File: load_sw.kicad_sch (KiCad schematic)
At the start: 47 parts, among them Q10 2N7002 TR PBFREE, Q11 MMBT3904, Q12 2N7002 TR PBFREE, Q4 2N7002 TR PBFREE, Q5 MMBT3904, Q6 2N7002 TR PBFREE, Q7 2N7002 TR PBFREE, Q8 MMBT3904, Q9 PSMN020-100YS, U10 LM5050-1, U9 TPS16851VMAR

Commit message: Working on layout
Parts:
- removed TP2: TP_PGOOD, TestPoint:TestPoint_Plated_Hole_D5.0mm, symbol Connector:TestPoint
- removed TP3: TP_FLTn, TestPoint:TestPoint_Plated_Hole_D5.0mm, symbol Connector:TestPoint

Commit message: Working on it
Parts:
- renumbered D1 to D3, D2 to D4, D3 to D5, D4 to D6, D5 to D7, D6 to D8, D7 to D9, Q11 to Q10, Q12 to Q11, Q4 to Q3, Q5 to Q4, Q6 to Q5, Q7 to Q6, Q8 to Q7, Q9 to Q8, Q10 to Q9, R27 to R25, R28 to R26, R29 to R27, R30 to R28, R31 to R29, R32 to R30, R33 to R31, R34 to R32, R35 to R33, R36 to R34, R37 to R35, R38 to R36, R39 to R37, R40 to R38, R41 to R39, R42 to R40, R43 to R41, R44 to R42, R45 to R43

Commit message: Working on schematic and layout
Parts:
- removed D5: LTST-C190KRKT, LED_SMD:LED_0603_1608Metric, symbol Device:LED
- removed D7: LTST-C170GKT, LED_SMD:LED_0805_2012Metric, symbol Device:LED
- removed D9: LTST-C190KFKT, LED_SMD:LED_0603_1608Metric, symbol Device:LED
- removed Q10, Q4, Q7: MMBT3904, Package_TO_SOT_SMD:TSOT-23, symbol Device:Q_NPN
- removed Q11, Q3, Q5, Q6, Q9: 2N7002 TR PBFREE, Package_TO_SOT_SMD:TSOT-23, symbol Transistor_FET:Q_NMOS_DGS
- removed R36, R38, R42: 1Meg, Resistor_SMD:R_0603_1608Metric, symbol Device:R_US
- removed R37, R40, R43: 21.5, Resistor_SMD:R_0603_1608Metric, symbol Device:R_US
- added Q3: 2N7002, Package_TO_SOT_SMD:SOT-23, symbol Transistor_FET:2N7002
- added R37: R, symbol Device:R
- U10: renamed from U9; Supplier_2 (none) -> JLCPCB; Supplier_2 P/N (none) -> C52742265; Supplier_2 Price @ Qty (none) -> 1; Supplier_2 Unit Price (none) -> 11.0758
- renumbered C58 to C60, C59 to C61, C60 to C62, C61 to C63, C62 to C64, C63 to C65, C64 to C66, C65 to C67, R25 to R26, R26 to R27, R27 to R28, R28 to R29, R29 to R30, R30 to R31, R31 to R32, R32 to R33, R33 to R34, R34 to R35, R35 to R36, R39 to R40, R41 to R42, U10 to U11
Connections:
- net EN: now also Q3.1 (G), R37.1
- net EN_UVLO: now also Q3.3 (D)
- net GND: now also Q3.2 (S), R37.2
- net SWEN: now reaches U10.20 (SWEN)
- no-connect marks 5 -> 4

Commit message: BOM in folder
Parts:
- removed R37: R, symbol Device:R
- added R24: 10k, Resistor_SMD:R_0603_1608Metric, symbol Device:R
- C60, C65: Supplier_1 Digikey -> LCSC; Supplier_1 P/N 490-GCM1885C2A101FA16DTR-ND -> C527967; Supplier_1 Unit Price 0.14000 -> (none)
- C61: JLCPCB Status (none) -> JLC in-stock package match; Mfr P/N GCM1885C2A100FA16D -> CL10C100JB8NNNC; Supplier_1 Digikey -> LCSC; Supplier_1 P/N 490-GCM1885C2A100FA16DTR-ND -> C1634; Supplier_1 Unit Price 0.14000 -> (none)
- C62: JLCPCB Status (none) -> JLC in-stock package match; Mfr P/N CC0603JRX7R9BB224 -> CL10B224KA8NNNC; Supplier_1 Digikey -> LCSC; Supplier_1 P/N 13-CC0603JRX7R9BB224TR-ND -> C21120; Supplier_1 Unit Price 0.15000 -> (none)
- C63: JLCPCB Status (none) -> JLC in-stock package match; Mfr P/N GCM1885C1H472FA16D -> 0603B472K500NT; Supplier_1 Digikey -> LCSC; Supplier_1 P/N 490-GCM1885C1H472FA16DTR-ND -> C53987; Supplier_1 Unit Price 0.18000 -> (none)
- C64: JLCPCB Status (none) -> JLC in-stock package match; Mfr P/N GCM1885C2A220FA16D -> CL10C220JB8NNNC; Supplier_1 Digikey -> LCSC; Supplier_1 P/N 490-16413-2-ND -> C1653; Supplier_1 Unit Price 0.14000 -> (none)
- C66: JLCPCB Status (none) -> JLC in-stock package match; Mfr P/N GCM21B5C1H223FA16L -> CL21B223KBANNNC; Supplier_1 Digikey -> LCSC; Supplier_1 P/N 490-GCM21B5C1H223FA16LTR-ND -> C1729; Supplier_1 Unit Price 0.52000 -> (none)
- C67: JLCPCB Status (none) -> JLC in-stock package match; Mfr P/N 06035C104K4T2A -> CC0603KRX7R9BB104; Supplier_1 Digikey -> LCSC; Supplier_1 P/N 478-KAM15AR71H104KTTR-ND -> C14663; Supplier_1 Unit Price 0.10000 -> (none)
- D3, D4: JLCPCB Status (none) -> Similar JLC in-stock package match; Mfr P/N TPSMB28CA-VR -> SMBJ28CA; Supplier_1 Digikey -> LCSC; Supplier_1 P/N TPSMB28CA-VRTR-ND -> C353369; Supplier_1 Unit Price 0.23000 -> (none)
- D6, D8: Supplier_1 Digikey -> LCSC; Supplier_1 P/N 1727-7326-2-ND -> C549269; Supplier_1 Unit Price 0.19000 -> (none)
- Q3: JLCPCB Status (none) -> Similar JLC in-stock package match; Mfr P/N (none) -> L2N7002SLLT1G; Supplier_1 (none) -> LCSC; Supplier_1 P/N (none) -> C22446827
- Q8: Supplier_1 Digikey -> LCSC; Supplier_1 P/N 1727-4286-2-ND -> C89867; Supplier_1 Unit Price 1.42000 -> (none)
- R26, R28: JLCPCB Status (none) -> JLC in-stock package match; Mfr P/N RNCF0603BKC1M00 -> 0603WAF1004T5E; Supplier_1 Digikey -> LCSC; Supplier_1 P/N RNCF0603BKC1M00TR-ND -> C22935; Supplier_1 Unit Price 0.11000 -> (none)
- R27: Supplier_1 Digikey -> LCSC; Supplier_1 P/N P36KDBTR-ND -> C473249; Supplier_1 Unit Price 0.10000 -> (none)
- R29: Supplier_1 Digikey -> LCSC; Supplier_1 P/N 2019-RN73R1JTTD6732B25TR-ND -> C2506885; Supplier_1 Unit Price 0.12000 -> (none)
- R30: JLCPCB Status (none) -> Similar JLC in-stock package match; Mfr P/N ERA-3AEB151V -> RC0603JR-07150RL; Supplier_1 Digikey -> LCSC; Supplier_1 P/N P150DBTR-ND -> C126805; Supplier_1 Unit Price 0.10000 -> (none)
- R31: JLCPCB Status (none) -> JLC in-stock package match; Mfr P/N ERA-3AEB244V -> 0603WAF2403T5E; Supplier_1 Digikey -> LCSC; Supplier_1 P/N P240KDBTR-ND -> C4197; Supplier_1 Unit Price 0.10000 -> (none)
- R32, R33: JLCPCB Status (none) -> JLC in-stock package match; Mfr P/N ERA-3AEB333V -> 0603WAF3302T5E; Supplier_1 Digikey -> LCSC; Supplier_1 P/N P33KDBTR-ND -> C4216; Supplier_1 Unit Price 0.10000 -> (none)
- R34: Supplier_1 (none) -> LCSC; Supplier_1 P/N (none) -> C23179
- R35: JLCPCB Status (none) -> Similar JLC in-stock package match; Mfr P/N (none) -> FRC0603F4642TS; Supplier_1 (none) -> LCSC; Supplier_1 P/N (none) -> C3013203
- R36: JLCPCB Status (none) -> JLC in-stock package match; Mfr P/N (none) -> 0603WAF1001T5E; Supplier_1 (none) -> LCSC; Supplier_1 P/N (none) -> C21190
- R40: Supplier_1 Digikey -> LCSC; Supplier_1 P/N RTAN1206BKE10R0TR-ND -> C17888; Supplier_1 Unit Price 0.42000 -> (none)
- R42: JLCPCB Status (none) -> JLC in-stock package match; Mfr P/N ERA-3AEB101V -> RC0603FR-07100RL; Supplier_1 Digikey -> LCSC; Supplier_1 P/N P100DBTR-ND -> C105588; Supplier_1 Unit Price 0.10000 -> (none)
- U10: Supplier_1 Texas Instruments -> LCSC; Supplier_1 P/N TPS16851VMAR -> C48705346; Supplier_1 Unit Price 10.32 -> (none)
- U11: JLCPCB Status (none) -> JLC in-stock package match; Mfr P/N (none) -> LM5050MKX-1/NOPB; Supplier_1 (none) -> LCSC; Supplier_1 P/N (none) -> C473393
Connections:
- net +3V3: now also R24.1
- net EN: now also R24.2

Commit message: to be done: silk screen and ezzat review
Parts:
- C63: footprint Resistor_SMD:R_0603_1608Metric -> Capacitor_SMD:C_0603_1608Metric
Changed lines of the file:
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@@
 	)
 	(symbol
-		(lib_id "power:+3V3")
-		(at 38.1 102.87 0)
-		(unit 1)
-		(exclude_from_sim no)
-		(in_bom yes)
-		(on_board yes)
-		(dnp no)
-		(fields_autoplaced yes)
-		(property "Reference" "#PWR0107"
-			(at 38.1 106.68 0)
-			(effects
-				(font
-					(size 1.27 1.27)
-				)
-				(hide yes)
-			)
-		)
-		(property "Value" "+3V3"
-			(at 38.1 97.79 0)
-			(effects
-				(font
-					(size 1.27 1.27)
-				)
-			)
-		)
-		(property "Footprint" ""
-			(at 38.1 102.87 0)
-			(effects
-				(font
-					(size 1.27 1.27)
-				)
-				(hide yes)
-			)
-		)
-		(property "Datasheet" ""
-			(at 38.1 102.87 0)
-			(effects
-				(font
-					(size 1.27 1.27)
-				)
-				(hide yes)
-			)
-		)
-		(property "Description" "Power symbol creates a global label with name \"+3V3\""
-			(at 38.1 102.87 0)
-			(effects
-				(font
-					(size 1.27 1.27)
-				)
-				(hide yes)
-			)
-		)
-		(pin "1"
-		)
-		(instances
-			(project "PowerBoard"
-				(path "/99785679-20de-4827-b4cc-bc3c187068c9/9564929a-642e-4163-88c2-45054b63a5ed/6815ee12-689e-4386-87ac-9bb461f0a023"
-					(reference "#PWR0107")
-					(unit 1)
-				)
-				(path "/99785679-20de-4827-b4cc-bc3c187068c9/9564929a-642e-4163-88c2-45054b63a5ed/b04f366d-f95e-45dc-bbbe-449492e7a2e8"
-					(reference "#PWR0109")
-					(unit 1)
-				)
-			)
-		)
-	)
-	(symbol
 		(lib_id "Device:R_US")
 		(at 74.93 76.2 0)
@@
 	)
 	(symbol
+		(lib_id "power:+3V3")
+		(at 38.1 102.87 0)
+		(unit 1)
+		(exclude_from_sim no)
+		(in_bom yes)
+		(on_board yes)
+		(dnp no)
+		(fields_autoplaced yes)
+		(property "Reference" "#PWR0107"
+			(at 38.1 106.68 0)
+			(effects
+				(font
+					(size 1.27 1.27)
+				)
+				(hide yes)
+			)
+		)
+		(property "Value" "+3V3"
+			(at 38.1 97.79 0)
+			(effects
+				(font
+					(size 1.27 1.27)
+				)
+			)
+		)
+		(property "Footprint" ""
+			(at 38.1 102.87 0)
+			(effects
+				(font
+					(size 1.27 1.27)
+				)
+				(hide yes)
+			)
+		)
+		(property "Datasheet" ""
+			(at 38.1 102.87 0)
+			(effects
+				(font
+					(size 1.27 1.27)
+				)
+				(hide yes)
+			)
+		)
+		(property "Description" "Power symbol creates a global label with name \"+3V3\""
+			(at 38.1 102.87 0)
+			(effects
+				(font
+					(size 1.27 1.27)
+				)
+				(hide yes)
+			)
+		)
+		(pin "1"
+		)
+		(instances
+			(project "PowerBoard"
+				(path "/99785679-20de-4827-b4cc-bc3c187068c9/9564929a-642e-4163-88c2-45054b63a5ed/6815ee12-689e-4386-87ac-9bb461f0a023"
+					(reference "#PWR0107")
+					(unit 1)
+				)
+				(path "/99785679-20de-4827-b4cc-bc3c187068c9/9564929a-642e-4163-88c2-45054b63a5ed/b04f366d-f95e-45dc-bbbe-449492e7a2e8"
+					(reference "#PWR0109")
+					(unit 1)
+				)
+			)
+		)
+	)
+	(symbol
 		(lib_id "power:GND")
 		(at 223.52 82.55 0)
@@
 			)
 		)
-		(property "Footprint" "Resistor_SMD:R_0603_1608Metric"
+		(property "Footprint" "Capacitor_SMD:C_0603_1608Metric"
 			(at 157.1752 82.55 0)
 			(effects

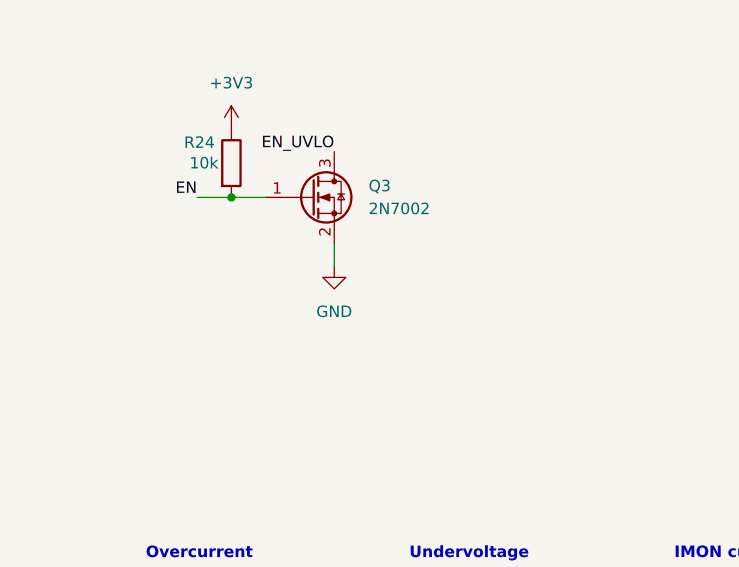
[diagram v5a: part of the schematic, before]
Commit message: Schematic updates
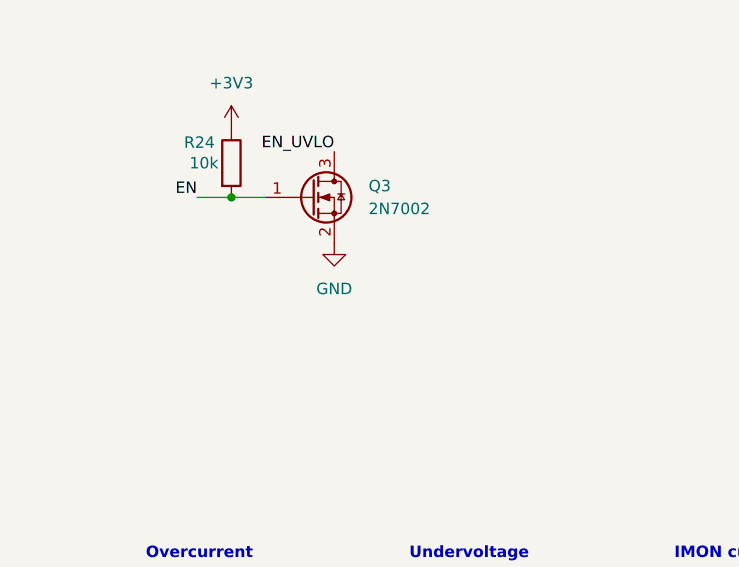
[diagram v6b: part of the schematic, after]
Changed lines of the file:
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@@
 		)
 	)
-	(wire
-		(pts
-			(xy 49.53 118.11) (xy 49.53 115.57)
-		)
-		(stroke
-			(width 0)
-			(type default)
-		)
-	)
 	(bus
 		(pts
@@
 		(lib_name "GND_4")
 		(lib_id "power:GND")
-		(at 49.53 118.11 0)
+		(at 49.53 115.57 0)
 		(unit 1)
 		(exclude_from_sim no)
@@
 		(fields_autoplaced yes)
 		(property "Reference" "#PWR01"
-			(at 49.53 124.46 0)
+			(at 49.53 121.92 0)
 			(effects
 				(font
@@
 		)
 		(property "Value" "GND"
-			(at 49.53 123.19 0)
+			(at 49.53 120.65 0)
 			(effects
 				(font
@@
 		)
 		(property "Footprint" ""
-			(at 49.53 118.11 0)
+			(at 49.53 115.57 0)
 			(effects
 				(font
@@
 		)
 		(property "Datasheet" ""
-			(at 49.53 118.11 0)
+			(at 49.53 115.57 0)
 			(effects
 				(font
@@
 		)
 		(property "Description" "Power symbol creates a global label with name \"GND\" , ground"
-			(at 49.53 118.11 0)
+			(at 49.53 115.57 0)
 			(effects
 				(font
@@
 		)
 		(property "Mfr" ""
-			(at 49.53 118.11 0)
+			(at 49.53 115.57 0)
 			(effects
 				(font
@@
 		)
 		(property "Mfr P/N" ""
-			(at 49.53 118.11 0)
+			(at 49.53 115.57 0)
 			(effects
 				(font
@@
 		)
 		(property "Supplier_1" ""
-			(at 49.53 118.11 0)
+			(at 49.53 115.57 0)
 			(effects
 				(font
@@
 		)
 		(property "Supplier_1 P/N" ""
-			(at 49.53 118.11 0)
+			(at 49.53 115.57 0)
 			(effects
 				(font
@@
 		)
 		(property "Supplier_1 Unit Price" ""
-			(at 49.53 118.11 0)
+			(at 49.53 115.57 0)
 			(effects
 				(font
@@
 		)
 		(property "Supplier_1 Price @ Qty" ""
-			(at 49.53 118.11 0)
+			(at 49.53 115.57 0)
 			(effects
 				(font
@@
 		)
 		(property "Supplier_2" ""
-			(at 49.53 118.11 0)
+			(at 49.53 115.57 0)
 			(effects
 				(font
@@
 		)
 		(property "Supplier_2 P/N" ""
-			(at 49.53 118.11 0)
+			(at 49.53 115.57 0)
 			(effects
 				(font
@@
 		)
 		(property "Supplier_2 Unit Price" ""
-			(at 49.53 118.11 0)
+			(at 49.53 115.57 0)
 			(effects
 				(font
@@
 		)
 		(property "Supplier_2 Price @ Qty" ""
-			(at 49.53 118.11 0)
+			(at 49.53 115.57 0)
 			(effects
 				(font
@@
 			)
 		)
+		(property "Mfr" ""
+			(at 46.99 110.49 0)
+			(effects
+				(font
+					(size 1.27 1.27)
+				)
+				(hide yes)
+			)
+		)
+		(property "Supplier_1 Unit Price" ""
+			(at 46.99 110.49 0)
+			(effects
+				(font
+					(size 1.27 1.27)
+				)
+				(hide yes)
+			)
+		)
+		(property "Supplier_1 Price @ Qty" ""
+			(at 46.99 110.49 0)
+			(effects
+				(font
+					(size 1.27 1.27)
+				)
+				(hide yes)
+			)
+		)
+		(property "Supplier_2" ""
+			(at 46.99 110.49 0)
+			(effects
+				(font
+					(size 1.27 1.27)
+				)
+				(hide yes)
+			)
+		)
+		(property "Supplier_2 P/N" ""
+			(at 46.99 110.49 0)
+			(effects
+				(font
+					(size 1.27 1.27)
+				)
+				(hide yes)
+			)
+		)
+		(property "Supplier_2 Unit Price" ""
+			(at 46.99 110.49 0)
+			(effects
+				(font
+					(size 1.27 1.27)
+				)
+				(hide yes)
+			)
+		)
+		(property "Supplier_2 Price @ Qty" ""
+			(at 46.99 110.49 0)
+			(effects
+				(font
+					(size 1.27 1.27)
+				)
+				(hide yes)
+			)
+		)
 		(pin "2"
 		)
@@
 			(at 223.52 68.58 0)
 			(effects
+				(font
+					(size 1.27 1.27)
+				)
+				(hide yes)
+			)
+		)
+		(property "Mfr" ""
+			(at 223.52 68.58 0)
+			(effects
+				(font
+					(size 1.27 1.27)
+				)
+				(hide yes)
+			)
+		)
+		(property "Supplier_1 Unit Price" ""
+			(at 223.52 68.58 0)
+			(effects
+				(font
+					(size 1.27 1.27)
+				)
+				(hide yes)
+			)
+		)
+		(property "Supplier_1 Price @ Qty" ""
+			(at 223.52 68.58 0)
+			(effects
+				(font
+					(size 1.27 1.27)
+				)
+				(hide yes)
+			)
+		)
+		(property "Supplier_2" ""
+			(at 223.52 68.58 0)
+			(effects
+				(font
+					(size 1.27 1.27)
+				)
+				(hide yes)
+			)
+		)
+		(property "Supplier_2 P/N" ""
+			(at 223.52 68.58 0)
+			(effects
+				(font
+					(size 1.27 1.27)
+				)
+				(hide yes)
+			)
+		)
+		(property "Supplier_2 Unit Price" ""
+			(at 223.52 68.58 0)
+			(effects
+				(font
+					(size 1.27 1.27)
+				)
+				(hide yes)
+			)
+		)
+		(property "Supplier_2 Price @ Qty" ""
+			(at 223.52 68.58 0)
+			(effects

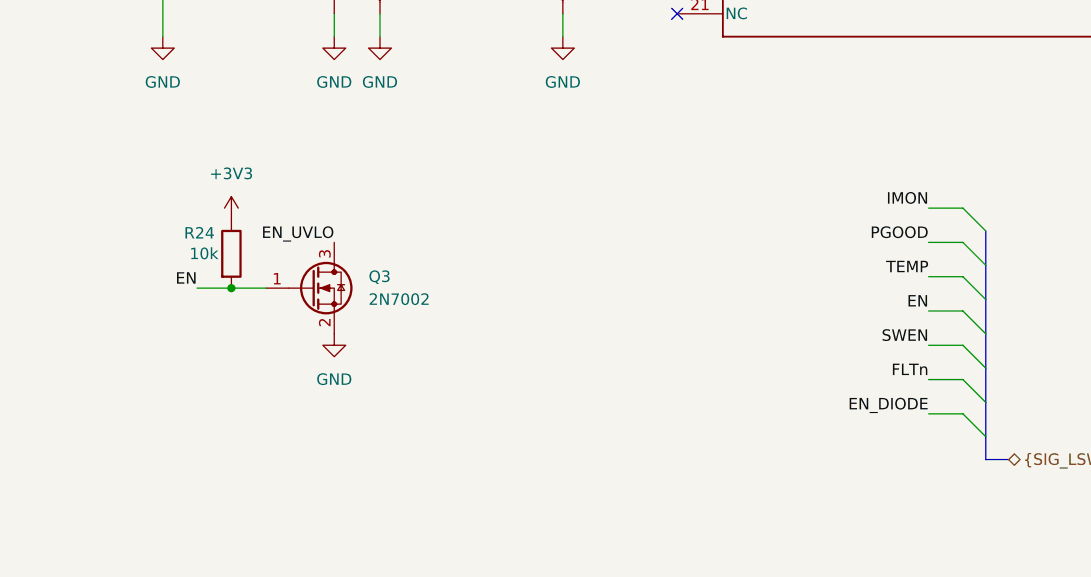
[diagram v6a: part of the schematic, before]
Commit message: i2c 0 and 1 bus routed + mosfet logic change
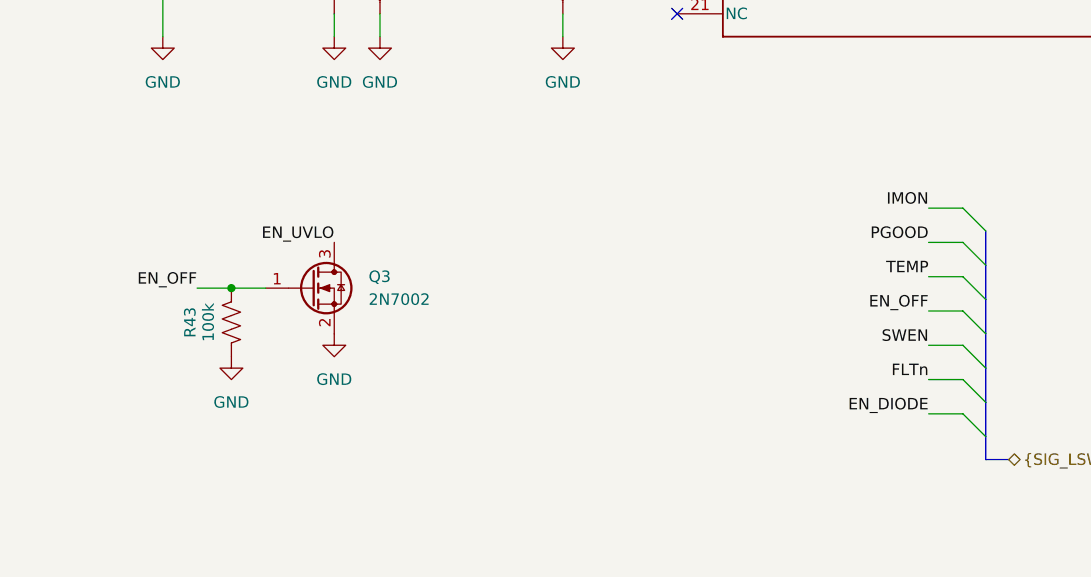
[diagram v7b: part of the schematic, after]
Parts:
- removed R24: 10k, Resistor_SMD:R_0603_1608Metric, symbol Device:R
- added R43: 100k, Resistor_SMD:R_0603_1608Metric, symbol Device:R_US
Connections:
- net GND: now also R43.2
- net EN renamed EN_OFF
- net EN_OFF: now also R43.1
